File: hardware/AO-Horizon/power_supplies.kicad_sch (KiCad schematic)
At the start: 17 parts

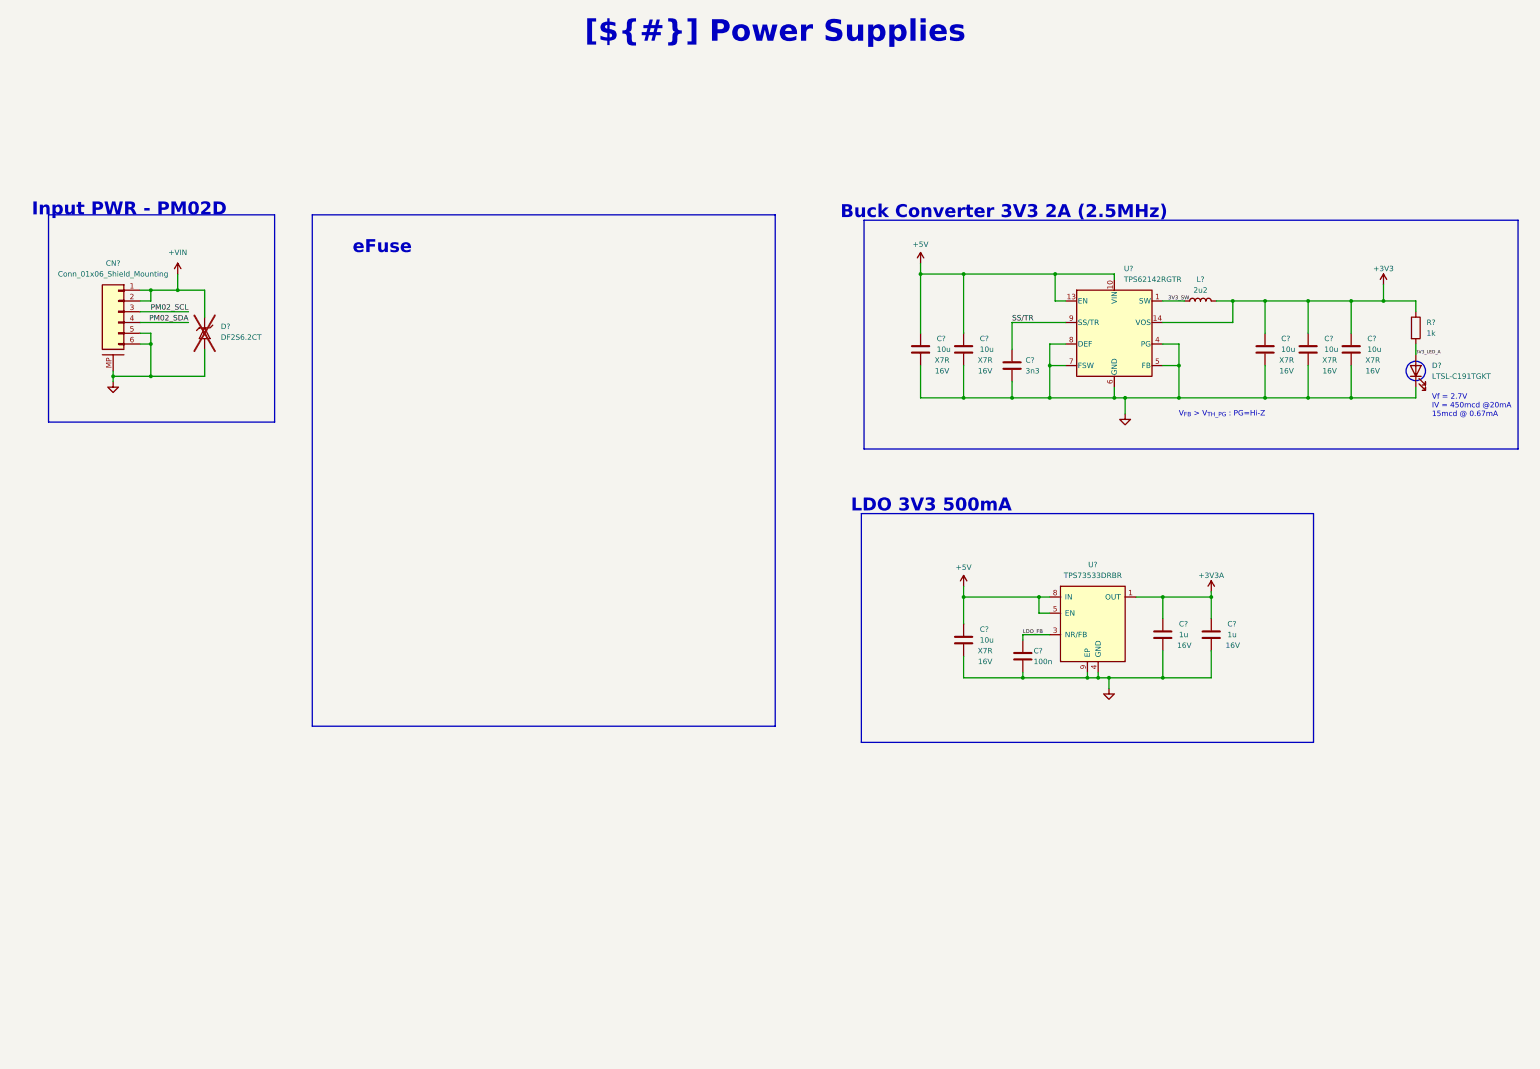
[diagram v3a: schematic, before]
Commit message: feat(library): add TPS16412 eFuse and restyle library to KLC (#11)
* docs(readme): simplify workflow diagram explanation

Mark DRAFT as under review, sync CHECK label, and add a colour key in README and template.

Co-Authored-By: Claude Sonnet 5.5 <noreply@anthropic.com>

* Update settings.json

* change spec file name

* update git-workflow skill

* change skill name by add hw-*

* docs: update AeroOptix-Horizon hardware spec

* docs: consolidate hardware handoff into checklist

* Update CLAUDE.md

* Update CLAUDE.md

* Update CLAUDE.md

* feat(hooks): replace protect hook with rule-based v2

Move file-protection rules into hooks/protect.json (allow > deny > ask)
and use ask for editable-with-approval files instead of a hard block.
Bash/PowerShell checks now inspect write targets, not any mention of a
protected path. Align settings.json permissions and drop the old hook.

Co-Authored-By: Claude Sonnet 5.5 <noreply@anthropic.com>

* docs: update CLAUDE.md for protection tiers and skill names

Describe the ask/deny protection rules, the v2 hook and protect.json,
and fix stale skill and template names.

Co-Authored-By: Claude Sonnet 5.5 <noreply@anthropic.com>

* Update .gitignore

* Update .gitignore

* Update .gitignore

* del skills

* Update engineering.md

* Update git-workflow.md

* Update hardware-workflow.md

* Update settings.json

* Update pull_request_template.md

* Update .gitignore

* Update .gitignore

* Delete SKILL.md

* Delete SKILL.md

* Update .gitignore

* add git-workflow skill

* Update CLAUDE.md

* Update protect.json

* Update settings.json

* Create MEMORY.md

* feat(agents): add codex-hw-delegate for bounded Codex tasks

Add a project agent that delegates one small, read-only-by-default task
to Codex CLI. It gates trivial or ambiguous requests, refuses PDF and
KiCad file contents, never mutates git, cross-checks Codex output and
returns a fixed report format.

Co-Authored-By: Claude Sonnet 5.5 <noreply@anthropic.com>

* fix(hooks): resolve ..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
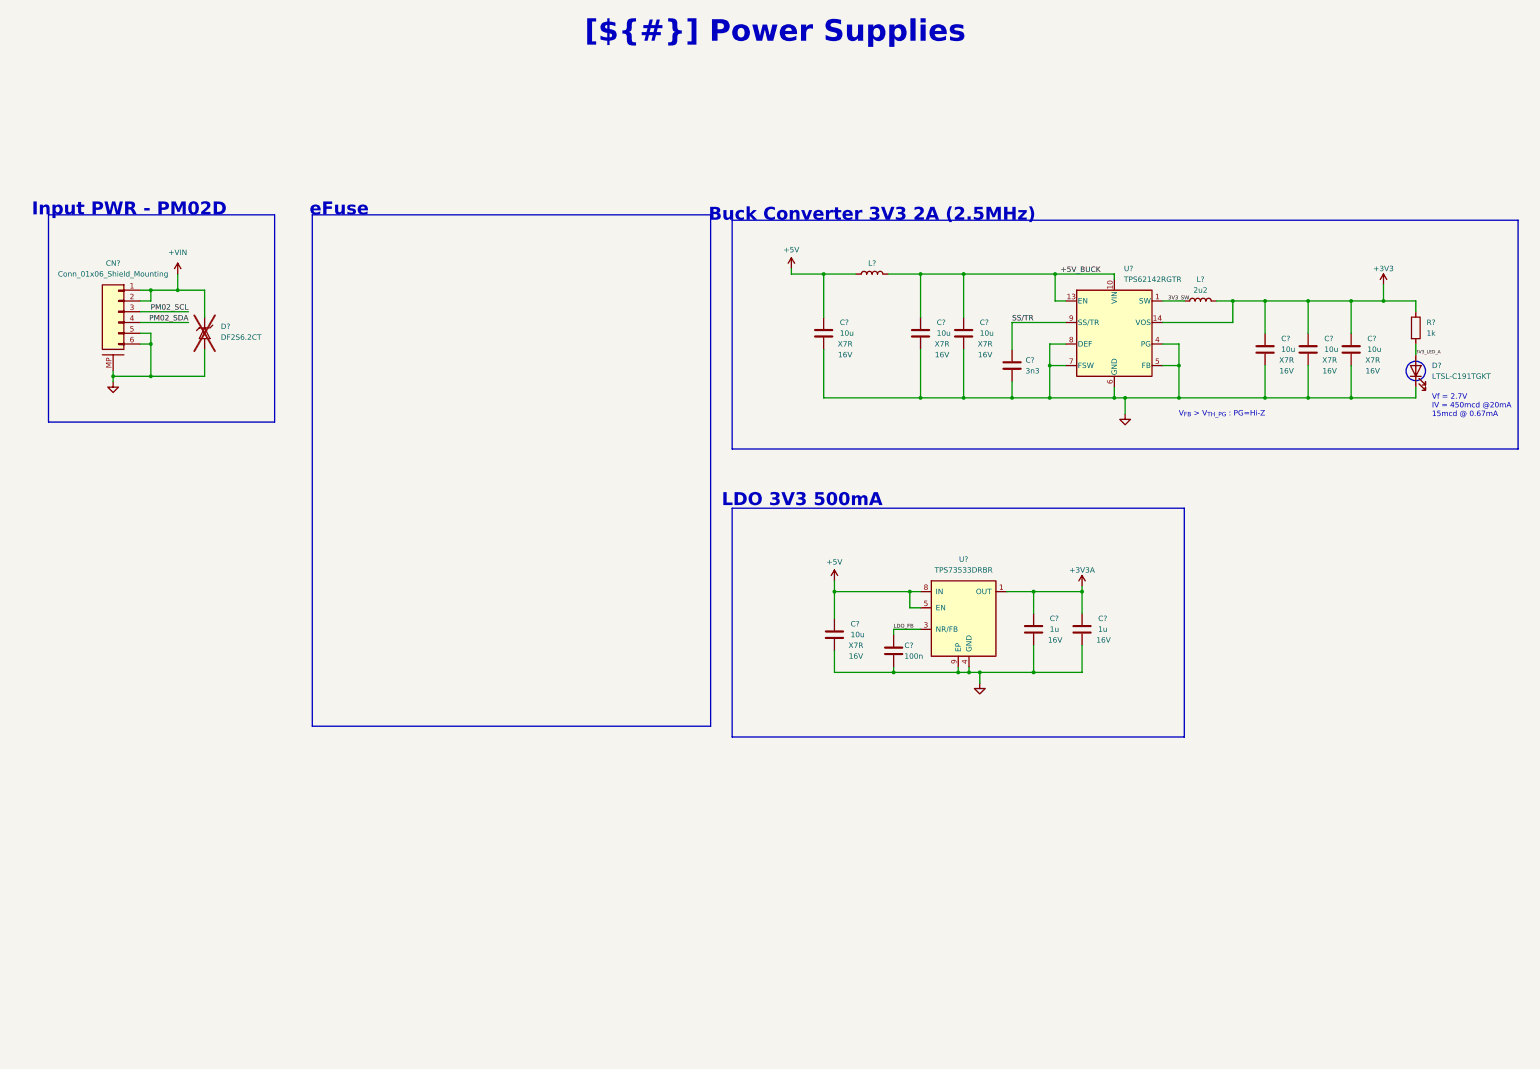
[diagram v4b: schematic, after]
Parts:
- added C?: 10u, 0_Capacitor_SMD:C_0805_2012Metric_NomDensity, symbol Device:C
- added L?: (no value), symbol Device:L
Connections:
- net +5V: now also C?.1, L?.1; no longer C?.1, C?.1, U?.10 (VIN), U?.11 (VIN), U?.12 (VIN), U?.13 (EN)
- net GND: now also C?.2
- new net +5V_BUCK: C?.1, C?.1, L?.2, U?.10 (VIN), U?.11 (VIN), U?.12 (VIN), U?.13 (EN)
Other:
- moved on the sheet: C?, U?

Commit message: feat: switch magnetometer to IST8310, add eFuse and draft pins (#13)
* docs(readme): simplify workflow diagram explanation

Mark DRAFT as under review, sync CHECK label, and add a colour key in README and template.

Co-Authored-By: Claude Sonnet 5.5 <noreply@anthropic.com>

* Update settings.json

* change spec file name

* update git-workflow skill

* change skill name by add hw-*

* docs: update AeroOptix-Horizon hardware spec

* docs: consolidate hardware handoff into checklist

* Update CLAUDE.md

* Update CLAUDE.md

* Update CLAUDE.md

* feat(hooks): replace protect hook with rule-based v2

Move file-protection rules into hooks/protect.json (allow > deny > ask)
and use ask for editable-with-approval files instead of a hard block.
Bash/PowerShell checks now inspect write targets, not any mention of a
protected path. Align settings.json permissions and drop the old hook.

Co-Authored-By: Claude Sonnet 5.5 <noreply@anthropic.com>

* docs: update CLAUDE.md for protection tiers and skill names

Describe the ask/deny protection rules, the v2 hook and protect.json,
and fix stale skill and template names.

Co-Authored-By: Claude Sonnet 5.5 <noreply@anthropic.com>

* Update .gitignore

* Update .gitignore

* Update .gitignore

* del skills

* Update engineering.md

* Update git-workflow.md

* Update hardware-workflow.md

* Update settings.json

* Update pull_request_template.md

* Update .gitignore

* Update .gitignore

* Delete SKILL.md

* Delete SKILL.md

* Update .gitignore

* add git-workflow skill

* Update CLAUDE.md

* Update protect.json

* Update settings.json

* Create MEMORY.md

* feat(agents): add codex-hw-delegate for bounded Codex tasks

Add a project agent that delegates one small, read-only-by-default task
to Codex CLI. It gates trivial or ambiguous requests, refuses PDF and
KiCad file contents, never mutates git, cross-checks Codex output and
returns a fixed report format.

Co-Authored-By: Claude Sonnet 5.5 <noreply@anthropic.com>

* fix(hooks): resolve 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
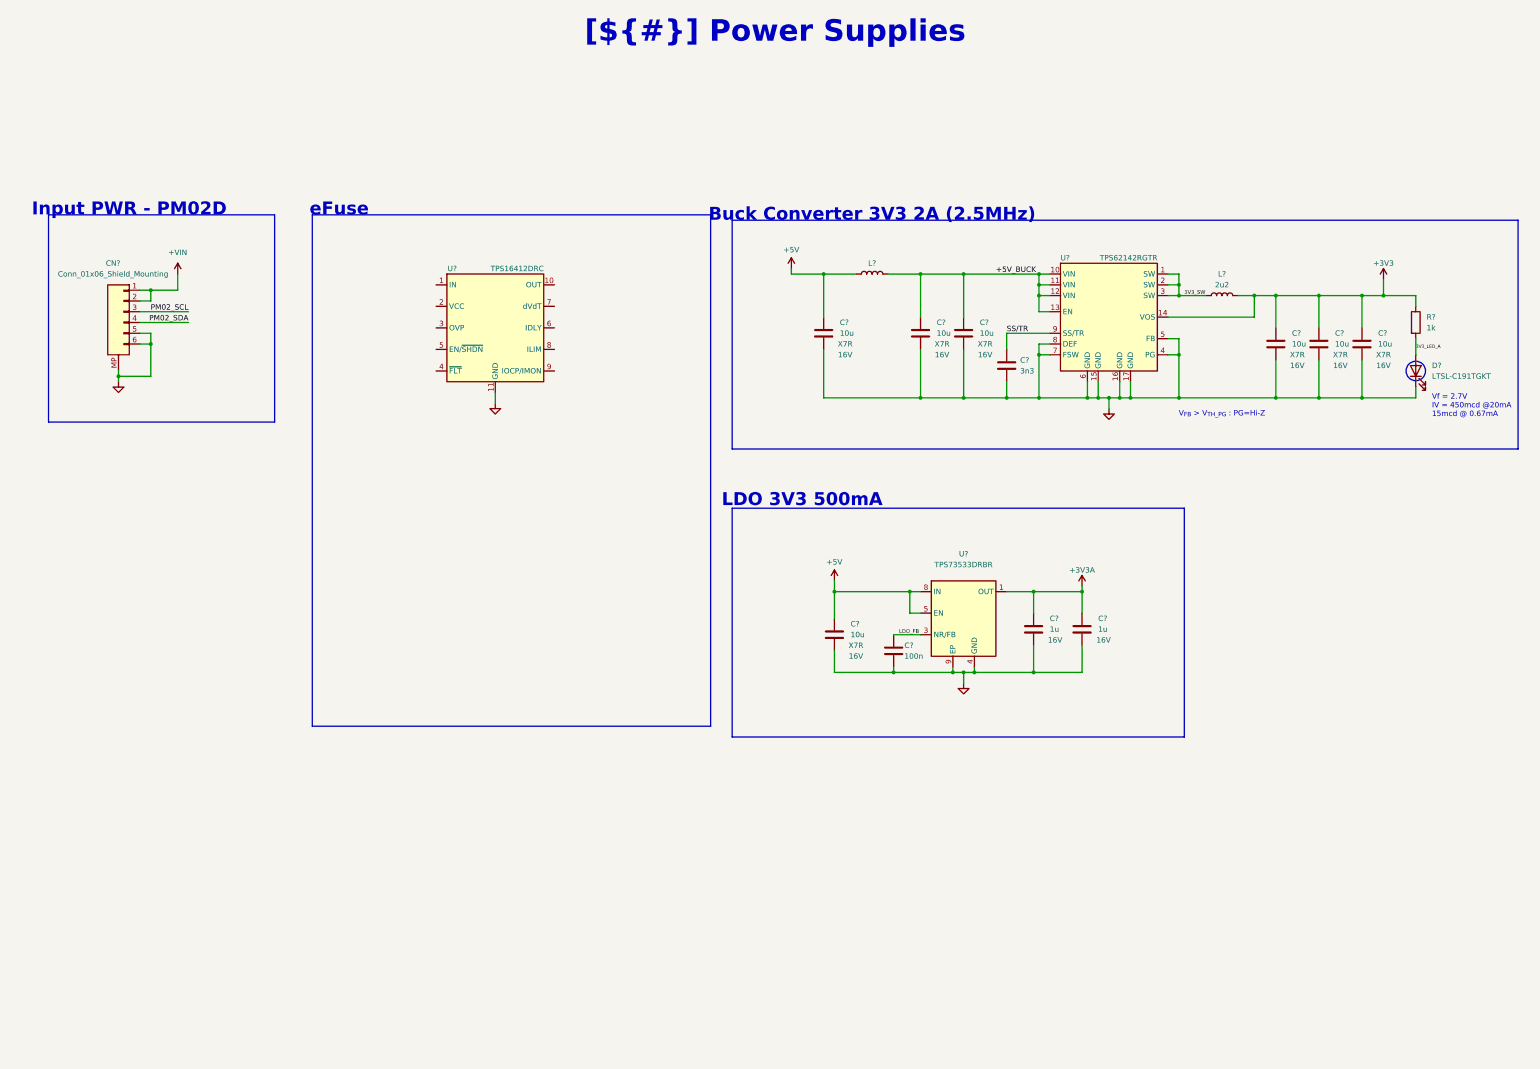
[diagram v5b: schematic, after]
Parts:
- removed D?: DF2S6.2CT, 0_Diode_SMD:D_SOD-882, symbol 0_Protection_ESD:DF2S6.2CT
- added U?: TPS16412DRC, 0_Package_SON:Texas_VSON-10-1EP_3x3mm_P0.5mm_EP1.65x2.4mm_ThermalVias, symbol 0_Protection_eFuse:TPS16412DRC
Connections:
- net GND: now also U?.11 (GND)
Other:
- moved on the sheet: C?, L?, R?

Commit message: feat(schematic): power sheet with wired eFuse, cleared block diagram, report PDF (#29)
* docs(readme): simplify workflow diagram explanation

Mark DRAFT as under review, sync CHECK label, and add a colour key in README and template.

Co-Authored-By: Claude Sonnet 5.5 <noreply@anthropic.com>

* Update settings.json

* change spec file name

* update git-workflow skill

* change skill name by add hw-*

* docs: update AeroOptix-Horizon hardware spec

* docs: consolidate hardware handoff into checklist

* Update CLAUDE.md

* Update CLAUDE.md

* Update CLAUDE.md

* feat(hooks): replace protect hook with rule-based v2

Move file-protection rules into hooks/protect.json (allow > deny > ask)
and use ask for editable-with-approval files instead of a hard block.
Bash/PowerShell checks now inspect write targets, not any mention of a
protected path. Align settings.json permissions and drop the old hook.

Co-Authored-By: Claude Sonnet 5.5 <noreply@anthropic.com>

* docs: update CLAUDE.md for protection tiers and skill names

Describe the ask/deny protection rules, the v2 hook and protect.json,
and fix stale skill and template names.

Co-Authored-By: Claude Sonnet 5.5 <noreply@anthropic.com>

* Update .gitignore

* Update .gitignore

* Update .gitignore

* del skills

* Update engineering.md

* Update git-workflow.md

* Update hardware-workflow.md

* Update settings.json

* Update pull_request_template.md

* Update .gitignore

* Update .gitignore

* Delete SKILL.md

* Delete SKILL.md

* Update .gitignore

* add git-workflow skill

* Update CLAUDE.md

* Update protect.json

* Update settings.json

* Create MEMORY.md

* feat(agents): add codex-hw-delegate for bounded Codex tasks

Add a project agent that delegates one small, read-only-by-default task
to Codex CLI. It gates trivial or ambiguous requests, refuses PDF and
KiCad file contents, never mutates git, cross-checks Codex output and
returns a fixed report format.

Co-Authored-By: Claude Sonnet 5.5 <noreply@anthropic.com>

* fi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
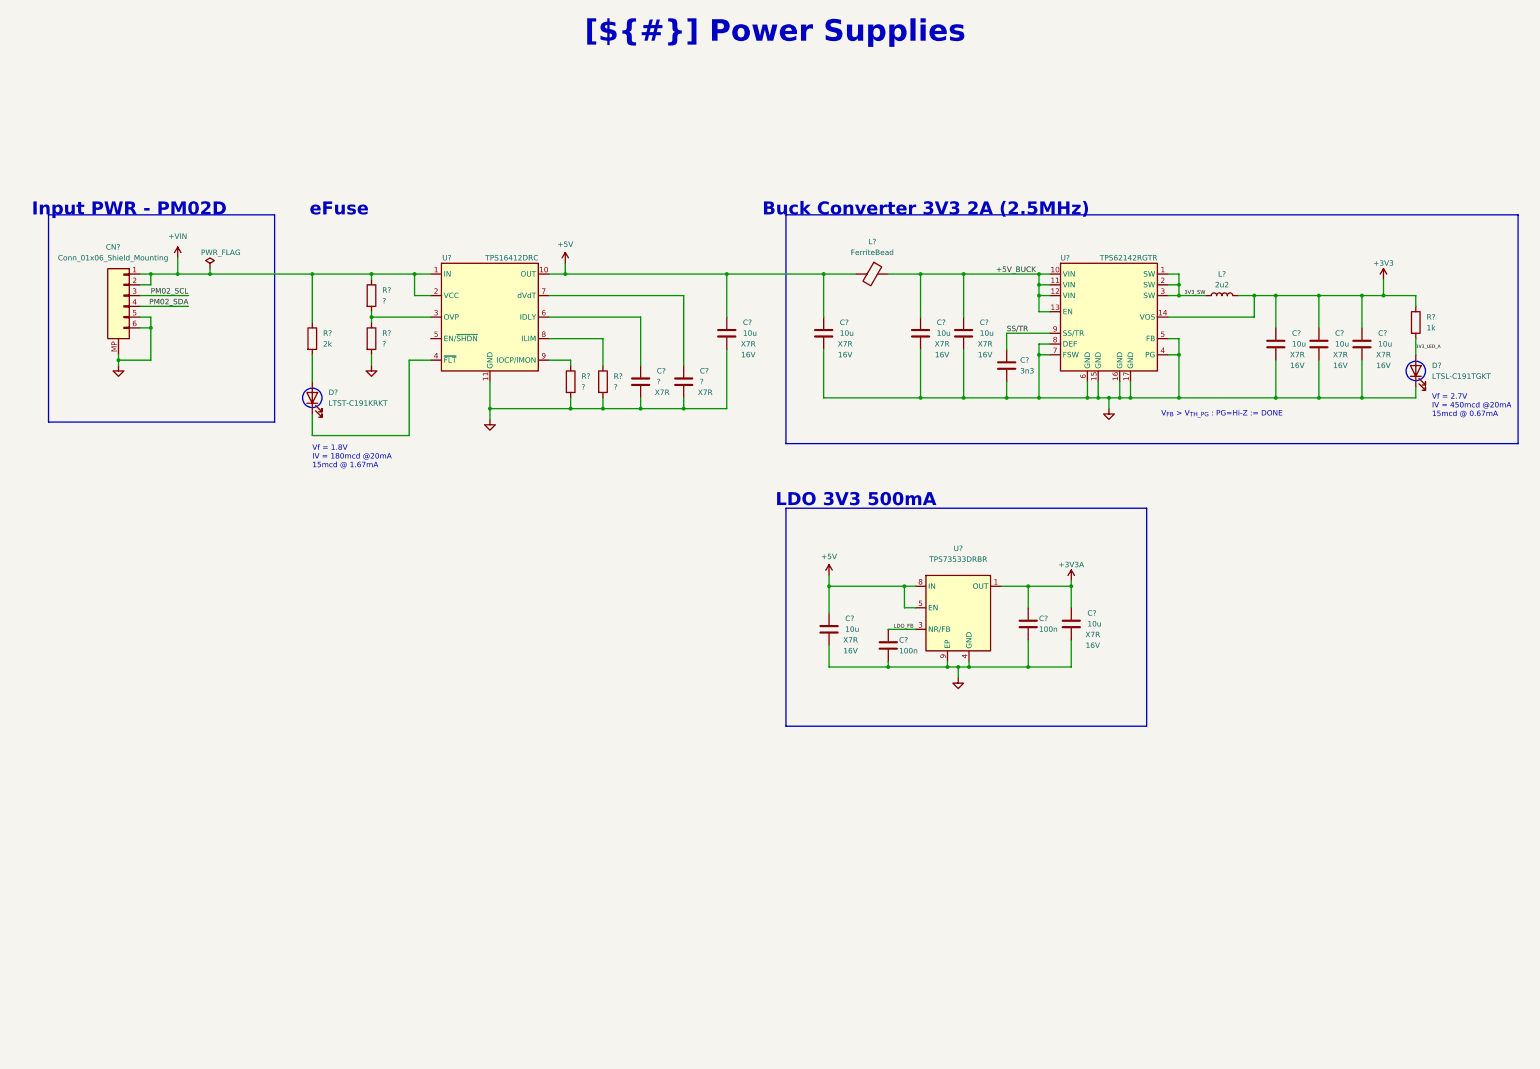
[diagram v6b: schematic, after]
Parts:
- removed C? (x2): 1u, 0_Capacitor_SMD:C_0603_1608Metric_NomDensity, symbol Device:C
- removed L?: (no value), symbol Device:L
- added C?: 100n, 0_Capacitor_SMD:C_0603_1608Metric_NomDensity, symbol Device:C
- added C? (x2): 10u, 0_Capacitor_SMD:C_0805_2012Metric_NomDensity, symbol Device:C
- added C? (x2): ?, symbol Device:C
- added D?: LTST-C191KRKT, 0_LED_SMD:LED_0603_1608Metric, symbol Device:LED
- added L?: FerriteBead, symbol Device:FerriteBead
- added R? (x4): ?, 0_Resistor_SMD:R_0603_1608Metric_NomDensity, symbol Device:R
- added R?: 2k, 0_Resistor_SMD:R_0603_1608Metric_NomDensity, symbol Device:R
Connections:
- net +3V3A: now also C?.1, C?.1
- net +5V: now also U?.10 (OUT), C?.1, L?.2
- net +5V_BUCK: now also L?.1
- net +VIN: now also U?.1 (IN), U?.2 (VCC), R?.1, R?.1
- net GND: now also C?.2, C?.2, C?.2, C?.2, C?.2, R?.2, R?.2, R?.2
- net at U?.3 (OVP): now also R?.1, R?.2
- net at U?.4 (~{FLT}): now also D?.1 (K)
- net at U?.6 (IDLY): now also C?.1
- net at U?.7 (dVdT): now also C?.1
- net at U?.8 (ILIM): now also R?.1
- net at U?.9 (IOCP/IMON): now also R?.1
- new net: D?.2 (A), R?.2
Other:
- note added: "V_{FB} > V_{TH_PG} : PG=Hi-Z := DONE"
- note added: "Vf = 1.8V IV = 180mcd @20mA 15mcd @ 1.67mA"
- note removed: "V_{FB} > V_{TH_PG} : PG=Hi-Z"
- moved on the sheet: C?, CN?, U?
